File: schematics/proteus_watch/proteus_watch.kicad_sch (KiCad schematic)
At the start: 0 parts

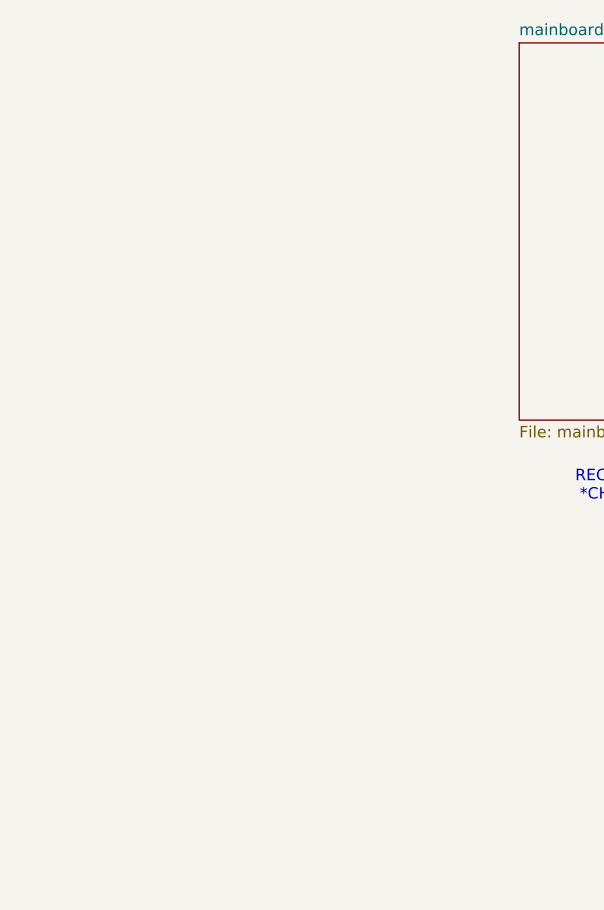
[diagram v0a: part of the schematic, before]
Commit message: v1.3
progress update with PCB layout. Repurposing old board design.
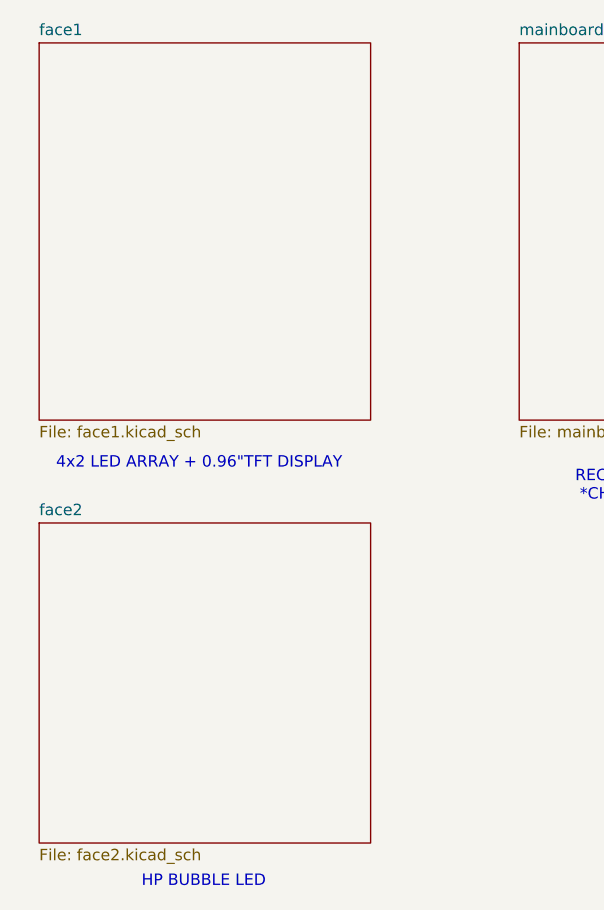
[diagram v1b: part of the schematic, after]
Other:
- added sheet face1 (face1.kicad_sch)
- added sheet face2 (face2.kicad_sch)
- note added: "4x2 LED ARRAY + 0.96"TFT DISPLAY"
- note added: "HP BUBBLE LED"
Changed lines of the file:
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@@
+		)
+	)
+	(text "4x2 LED ARRAY + 0.96\"TFT DISPLAY"
+		(exclude_from_sim no)
+		(at 91.44 122.936 0)
+		(effects
+			(font
+				(size 1.27 1.27)
+			)
+		)
+	)
+	(text "HP BUBBLE LED"
+		(exclude_from_sim no)
+		(at 91.948 169.418 0)
+		(effects
+			(font
+				(size 1.27 1.27)
+			)
 		)
 	)
@@
 	)
 	(sheet
+		(at 73.66 129.54)
+		(size 36.83 35.56)
+		(exclude_from_sim no)
+		(in_bom yes)
+		(on_board yes)
+		(dnp no)
+		(fields_autoplaced yes)
+		(stroke
+			(width 0.1524)
+			(type solid)
+		)
+		(fill
+			(color 0 0 0 0)
+		)
+		(property "Sheetname" "face2"
+			(at 73.66 128.8284 0)
+			(show_name no)
+			(do_not_autoplace no)
+			(effects
+				(font
+					(size 1.27 1.27)
+				)
+				(justify left bottom)
+			)
+		)
+		(property "Sheetfile" "face2.kicad_sch"
+			(at 73.66 165.6846 0)
+			(show_name no)
+			(do_not_autoplace no)
+			(effects
+				(font
+					(size 1.27 1.27)
+				)
+				(justify left top)
+			)
+		)
+		(instances
+			(project "proteus_watch"
+				(path "/51ea3200-1193-4241-98dd-8a7ea8639546"
+					(page "5")
+				)
+			)
+		)
+	)
+	(sheet
 		(at 127 76.2)
 		(size 38.1 41.91)
@@
 				)
 			)
+		)
+	)
+	(sheet
+		(at 73.66 76.2)
+		(size 36.83 41.91)
+		(exclude_from_sim no)
+		(in_bom yes)
+		(on_board yes)
+		(dnp no)
+		(fields_autoplaced yes)
+		(stroke
+			(width 0.1524)
+			(type solid)
+		)
+		(fill
+			(color 0 0 0 0)
+		)
+		(property "Sheetname" "face1"
+			(at 73.66 75.4884 0)
+			(show_name no)
+			(do_not_autoplace no)
+			(effects
+				(font
+					(size 1.27 1.27)
+				)
+				(justify left bottom)
+			)
+		)
+		(property "Sheetfile" "face1.kicad_sch"
+			(at 73.66 118.6946 0)
+			(show_name no)
+			(do_not_autoplace no)
+			(effects
+				(font
+					(size 1.27 1.27)
+				)
+				(justify left top)
+			)
+		)
+		(instances
+			(project "proteus_watch"
+				(path "/51ea3200-1193-4241-98dd-8a7ea8639546"
+					(page "4")
+				)
+			)

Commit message: v1.31
wip integrating face3
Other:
- added sheet face3 (face3.kicad_sch)
- note added: "HCMS-2901 DOT MATRIX DISPLAY"
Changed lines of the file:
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@@
+		)
+	)
+	(text "HCMS-2901 DOT MATRIX DISPLAY\n"
+		(exclude_from_sim no)
+		(at 91.186 32.512 0)
+		(effects
+			(font
+				(size 1.27 1.27)
+			)
 		)
 	)
@@
 				)
 			)
+		)
+	)
+	(sheet
+		(at 73.66 36.83)
+		(size 36.83 25.4)
+		(exclude_from_sim no)
+		(in_bom yes)
+		(on_board yes)
+		(dnp no)
+		(fields_autoplaced yes)
+		(stroke
+			(width 0.1524)
+			(type solid)
+		)
+		(fill
+			(color 0 0 0 0)
+		)
+		(property "Sheetname" "face3"
+			(at 73.66 36.1184 0)
+			(show_name no)
+			(do_not_autoplace no)
+			(effects
+				(font
+					(size 1.27 1.27)
+				)
+				(justify left bottom)
+			)
+		)
+		(property "Sheetfile" "face3.kicad_sch"
+			(at 73.66 62.8146 0)
+			(show_name no)
+			(do_not_autoplace no)
+			(effects
+				(font
+					(size 1.27 1.27)
+				)
+				(justify left top)
+			)
+		)
+		(instances
+			(project "proteus_watch"
+				(path "/51ea3200-1193-4241-98dd-8a7ea8639546"
+					(page "6")
+				)
+			)
